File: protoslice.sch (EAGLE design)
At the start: 1 part

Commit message: Added initial components
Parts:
- added JP1, JP2, JP3, JP4, JP5, JP6, JP7, JP8, JP9: (no value), pinhead:PINHD-2X14
- added SV1: (no value), con-lstb:MA10-2W
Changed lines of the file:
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@@
 <part name="U$1" library="amino" deviceset="XSLICE" device=""/>
 <part name="FRAME1" library="frames" deviceset="A3L-LOC" device=""/>
+<part name="JP1" library="pinhead" deviceset="PINHD-2X14" device=""/>
+<part name="JP2" library="pinhead" deviceset="PINHD-2X14" device=""/>
+<part name="JP3" library="pinhead" deviceset="PINHD-2X14" device=""/>
+<part name="JP4" library="pinhead" deviceset="PINHD-2X14" device=""/>
+<part name="JP5" library="pinhead" deviceset="PINHD-2X14" device=""/>
+<part name="JP6" library="pinhead" deviceset="PINHD-2X14" device=""/>
+<part name="JP7" library="pinhead" deviceset="PINHD-2X14" device=""/>
+<part name="JP8" library="pinhead" deviceset="PINHD-2X14" device=""/>
+<part name="SV1" library="con-lstb" deviceset="MA10-2W" device=""/>
+<part name="JP9" library="pinhead" deviceset="PINHD-2X14" device=""/>
 </parts>
 <sheets>
@@
 </plain>
 <instances>
-<instance part="U$1" gate="G$1" x="-2.54" y="0"/>
+<instance part="U$1" gate="G$1" x="2.54" y="81.28"/>
 <instance part="FRAME1" gate="G$1" x="-71.12" y="-91.44"/>
+<instance part="JP1" gate="A" x="35.56" y="93.98"/>
+<instance part="JP2" gate="A" x="58.42" y="93.98"/>
+<instance part="JP3" gate="A" x="81.28" y="93.98"/>
+<instance part="JP4" gate="A" x="104.14" y="93.98"/>
+<instance part="JP5" gate="A" x="127" y="93.98"/>
+<instance part="JP6" gate="A" x="152.4" y="93.98"/>
+<instance part="JP7" gate="A" x="177.8" y="93.98"/>
+<instance part="JP8" gate="A" x="203.2" y="93.98"/>
+<instance part="SV1" gate="1" x="248.92" y="93.98"/>
+<instance part="JP9" gate="A" x="226.06" y="93.98"/>
 </instances>
 <busses>

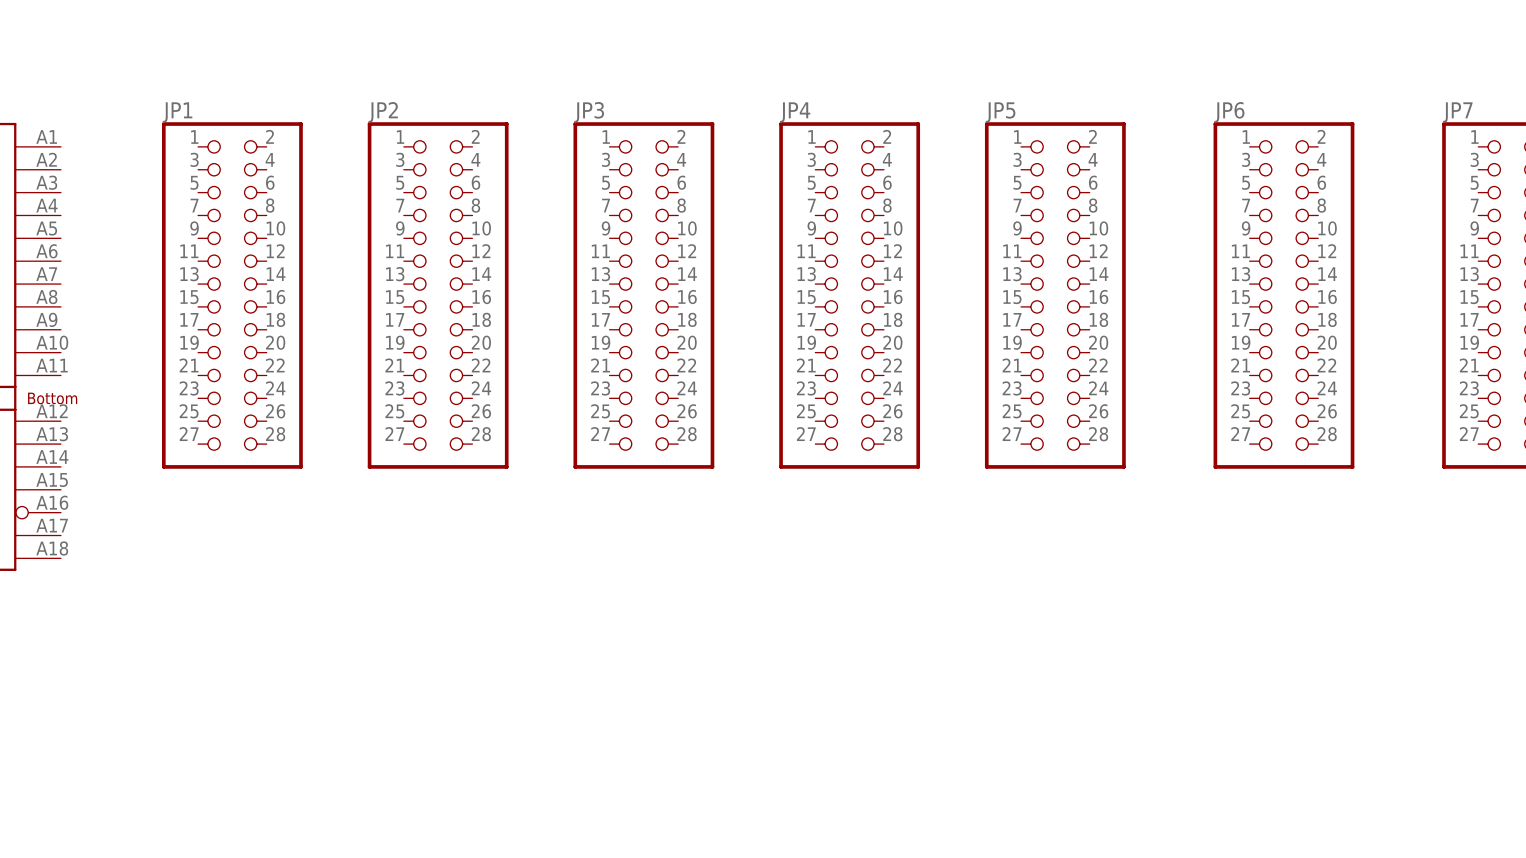
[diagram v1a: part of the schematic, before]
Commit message: Added passive components
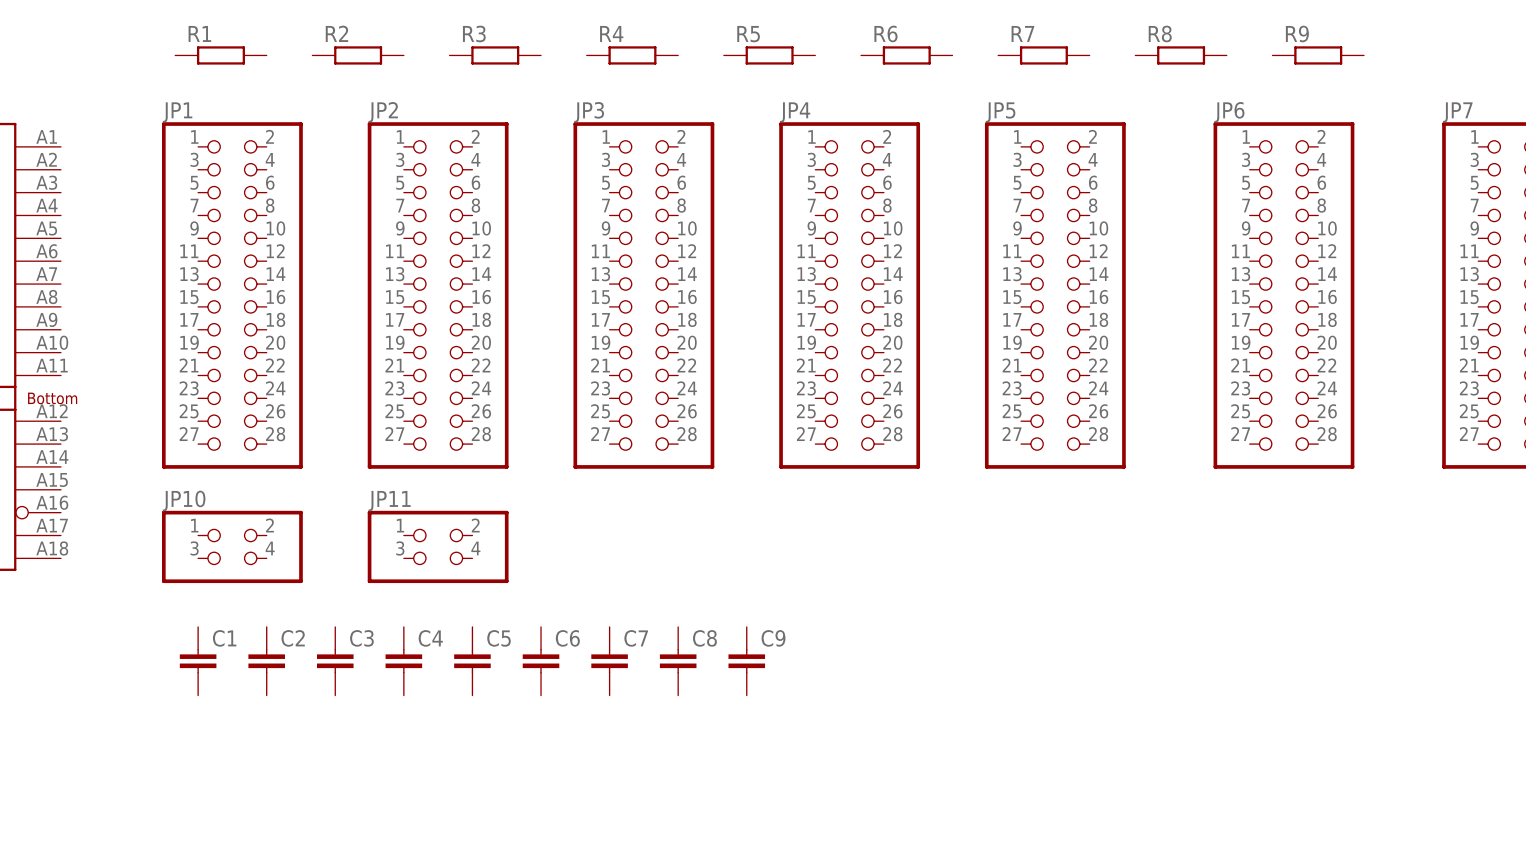
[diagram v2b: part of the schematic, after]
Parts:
- added C1, C2, C3, C4, C5, C6, C7, C8, C9: (no value), rcl:C-EUC0805
- added JP10, JP11: (no value), pinhead:PINHD-2X2
- added R1, R2, R3, R4, R5, R6, R7, R8, R9: (no value), rcl:R-EU_R0805
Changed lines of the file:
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@@
 <part name="SV1" library="con-lstb" deviceset="MA10-2W" device=""/>
 <part name="JP9" library="pinhead" deviceset="PINHD-2X14" device=""/>
+<part name="JP10" library="pinhead" deviceset="PINHD-2X2" device=""/>
+<part name="JP11" library="pinhead" deviceset="PINHD-2X2" device=""/>
+<part name="R1" library="rcl" deviceset="R-EU_" device="R0805"/>
+<part name="R2" library="rcl" deviceset="R-EU_" device="R0805"/>
+<part name="R3" library="rcl" deviceset="R-EU_" device="R0805"/>
+<part name="R4" library="rcl" deviceset="R-EU_" device="R0805"/>
+<part name="R5" library="rcl" deviceset="R-EU_" device="R0805"/>
+<part name="R6" library="rcl" deviceset="R-EU_" device="R0805"/>
+<part name="R7" library="rcl" deviceset="R-EU_" device="R0805"/>
+<part name="R8" library="rcl" deviceset="R-EU_" device="R0805"/>
+<part name="R9" library="rcl" deviceset="R-EU_" device="R0805"/>
+<part name="C1" library="rcl" deviceset="C-EU" device="C0805"/>
+<part name="C2" library="rcl" deviceset="C-EU" device="C0805"/>
+<part name="C3" library="rcl" deviceset="C-EU" device="C0805"/>
+<part name="C4" library="rcl" deviceset="C-EU" device="C0805"/>
+<part name="C5" library="rcl" deviceset="C-EU" device="C0805"/>
+<part name="C6" library="rcl" deviceset="C-EU" device="C0805"/>
+<part name="C7" library="rcl" deviceset="C-EU" device="C0805"/>
+<part name="C8" library="rcl" deviceset="C-EU" device="C0805"/>
+<part name="C9" library="rcl" deviceset="C-EU" device="C0805"/>
 </parts>
 <sheets>
@@
 <instance part="SV1" gate="1" x="248.92" y="93.98"/>
 <instance part="JP9" gate="A" x="226.06" y="93.98"/>
+<instance part="JP10" gate="A" x="38.1" y="63.5"/>
+<instance part="JP11" gate="A" x="60.96" y="63.5"/>
+<instance part="R1" gate="G$1" x="35.56" y="119.38"/>
+<instance part="R2" gate="G$1" x="50.8" y="119.38"/>
+<instance part="R3" gate="G$1" x="66.04" y="119.38"/>
+<instance part="R4" gate="G$1" x="81.28" y="119.38"/>
+<instance part="R5" gate="G$1" x="96.52" y="119.38"/>
+<instance part="R6" gate="G$1" x="111.76" y="119.38"/>
+<instance part="R7" gate="G$1" x="127" y="119.38"/>
+<instance part="R8" gate="G$1" x="142.24" y="119.38"/>
+<instance part="R9" gate="G$1" x="157.48" y="119.38"/>
+<instance part="C1" gate="G$1" x="33.02" y="53.34"/>
+<instance part="C2" gate="G$1" x="40.64" y="53.34"/>
+<instance part="C3" gate="G$1" x="48.26" y="53.34"/>
+<instance part="C4" gate="G$1" x="55.88" y="53.34"/>
+<instance part="C5" gate="G$1" x="63.5" y="53.34"/>
+<instance part="C6" gate="G$1" x="71.12" y="53.34"/>
+<instance part="C7" gate="G$1" x="78.74" y="53.34"/>
+<instance part="C8" gate="G$1" x="86.36" y="53.34"/>
+<instance part="C9" gate="G$1" x="93.98" y="53.34"/>
 </instances>
 <busses>

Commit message: Made for energy monitor proto
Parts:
- removed C1: (no value), rcl:C-EUC0805
- removed R1: (no value), rcl:R-EU_R0805
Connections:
- new net A1: JP11.1, U$1.A1
- new net A10: JP1.15, U$1.A10
- new net A11: JP1.17, U$1.A11
- new net A12: JP1.19, U$1.A12
- new net A13: JP1.21, U$1.A13
- new net A14: JP1.23, U$1.A14
- new net A15: JP1.25, U$1.A15
- new net A16: JP1.27, U$1.A16
- new net A17: JP10.1, U$1.A17
- new net A18: JP10.3, U$1.A18
- new net A2: JP11.3, U$1.A2
- new net A3: JP1.1, U$1.A3
- new net A4: JP1.3, U$1.A4
- new net A5: JP1.5, U$1.A5
- new net A6: JP1.7, U$1.A6
- new net A7: JP1.9, U$1.A7
- new net A8: JP1.11, U$1.A8
- new net A9: JP1.13, U$1.A9
- new net B1: JP11.2, U$1.B1
- new net B10: JP1.16, U$1.B10
- new net B11: JP1.18, U$1.B11
- new net B12: JP1.20, U$1.B12
- new net B13: JP1.22, U$1.B13
- new net B14: JP1.24, U$1.B14
- new net B15: JP1.26, U$1.B15
- new net B16: JP1.28, U$1.B16
- new net B17: JP10.2, U$1.B17
- new net B18: JP10.4, U$1.B18
- new net B2: JP11.4, U$1.B2
- new net B3: JP1.2, U$1.B3
- new net B4: JP1.4, U$1.B4
- new net B5: JP1.6, U$1.B5
- new net B6: JP1.8, U$1.B6
- new net B7: JP1.10, U$1.B7
- new net B8: JP1.12, U$1.B8
- new net B9: JP1.14, U$1.B9
- new net N$1: JP2.1, R2.1
- new net N$10: JP5.2, R5.2
- new net N$11: JP6.1, R6.1
- new net N$12: JP6.2, R6.2
- new net N$13: JP7.1, R7.1
- new net N$14: JP7.2, R7.2
- new net N$15: C7.1, JP7.27
- new net N$16: C7.2, JP7.28
- new net N$17: C6.2, JP6.28
- new net N$18: C6.1, JP6.27
- new net N$19: C5.2, JP5.28
- new net N$2: JP2.2, R2.2
- new net N$20: C5.1, JP5.27
- new net N$21: C4.2, JP4.28
- new net N$22: C4.1, JP4.27
- new net N$23: C3.2, JP3.28
- new net N$24: C3.1, JP3.27
- new net N$25: JP8.1, R8.1
- new net N$26: JP8.2, R8.2
- new net N$27: C8.1, JP8.27
- new net N$28: C8.2, JP8.28
- new net N$29: C9.1, JP9.27
- new net N$3: C2.1, JP2.27
- new net N$30: C9.2, JP9.28
- new net N$31: JP9.1, R9.1
- new net N$32: JP9.2, R9.2
- new net N$4: C2.2, JP2.28
- new net N$5: JP3.1, R3.1
- new net N$6: JP3.2, R3.2
- new net N$7: JP4.1, R4.1
- new net N$8: JP4.2, R4.2
- new net N$9: JP5.1, R5.1
- new net O1: JP9.5, SV1.20
- new net O10: JP9.23, SV1.2
- new net O11: JP9.6, SV1.19
- new net O12: JP9.8, SV1.17
- new net O13: JP9.10, SV1.15
- new net O14: JP9.12, SV1.13
- new net O15: JP9.14, SV1.11
- new net O16: JP9.16, SV1.9
- new net O17: JP9.18, SV1.7
- new net O18: JP9.20, SV1.5
- new net O19: JP9.22, SV1.3
- new net O2: JP9.7, SV1.18
- new net O20: JP9.24, SV1.1
- new net O3: JP9.9, SV1.16
- new net O4: JP9.11, SV1.14
- new net O5: JP9.13, SV1.12
- new net O6: JP9.15, SV1.10
- new net O7: JP9.17, SV1.8
- new net O8: JP9.19, SV1.6
- new net O9: JP9.21, SV1.4
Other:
- moved on the sheet: C2, C3, C4, C5, C6, C7, C8, C9, JP1, JP10, JP11, JP2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
